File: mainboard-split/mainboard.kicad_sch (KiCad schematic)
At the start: 24 parts, among them J1 3V3 IN, J2 Conn_01x04, J3 Conn_01x03, J4 Conn_01x02, J5 3V3 OUT, J6 STICK POWER, SW1 SW_SPDT_MSM, SW2 SW_SPDT_MSM, SW3 SW_Push, SW4 SW_Push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

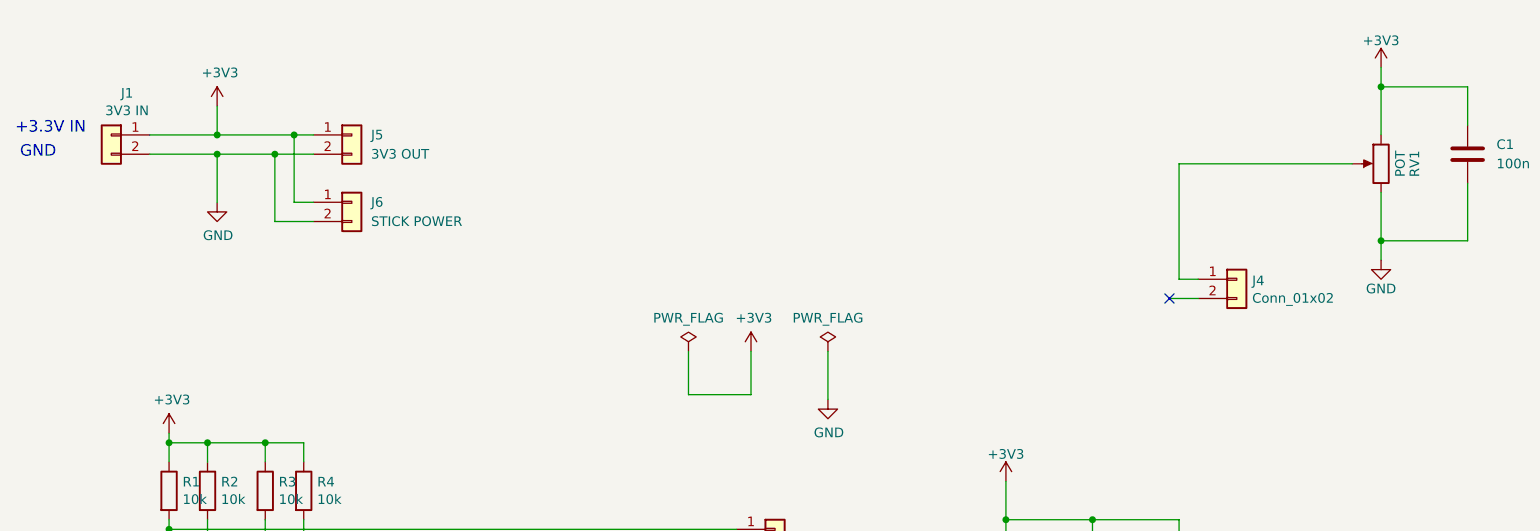
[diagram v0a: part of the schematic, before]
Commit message: Use Vref for pots and sticks.
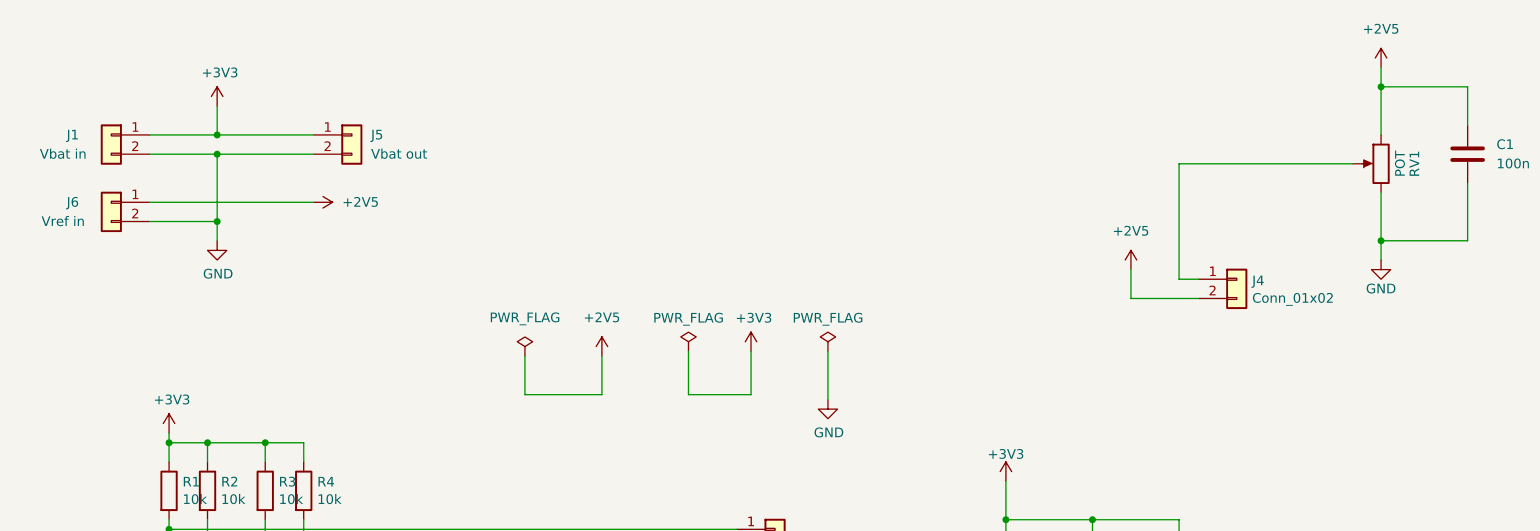
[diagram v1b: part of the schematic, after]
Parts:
- J1: value 3V3 IN -> Vbat in
- J5: value 3V3 OUT -> Vbat out
- J6: value STICK POWER -> Vref in
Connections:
- net +3V3: no longer C1.1, J6.1 (Pin_1), RV1.1
- net +2V5: now reaches J4.2 (Pin_2)
- net +2V5: now also C1.1, J6.1 (Pin_1), RV1.1
- no-connect marks 1 -> 0
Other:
- note removed: "+3.3V IN"
- note removed: "GND"
